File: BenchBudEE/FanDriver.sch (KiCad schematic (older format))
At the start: 0 parts

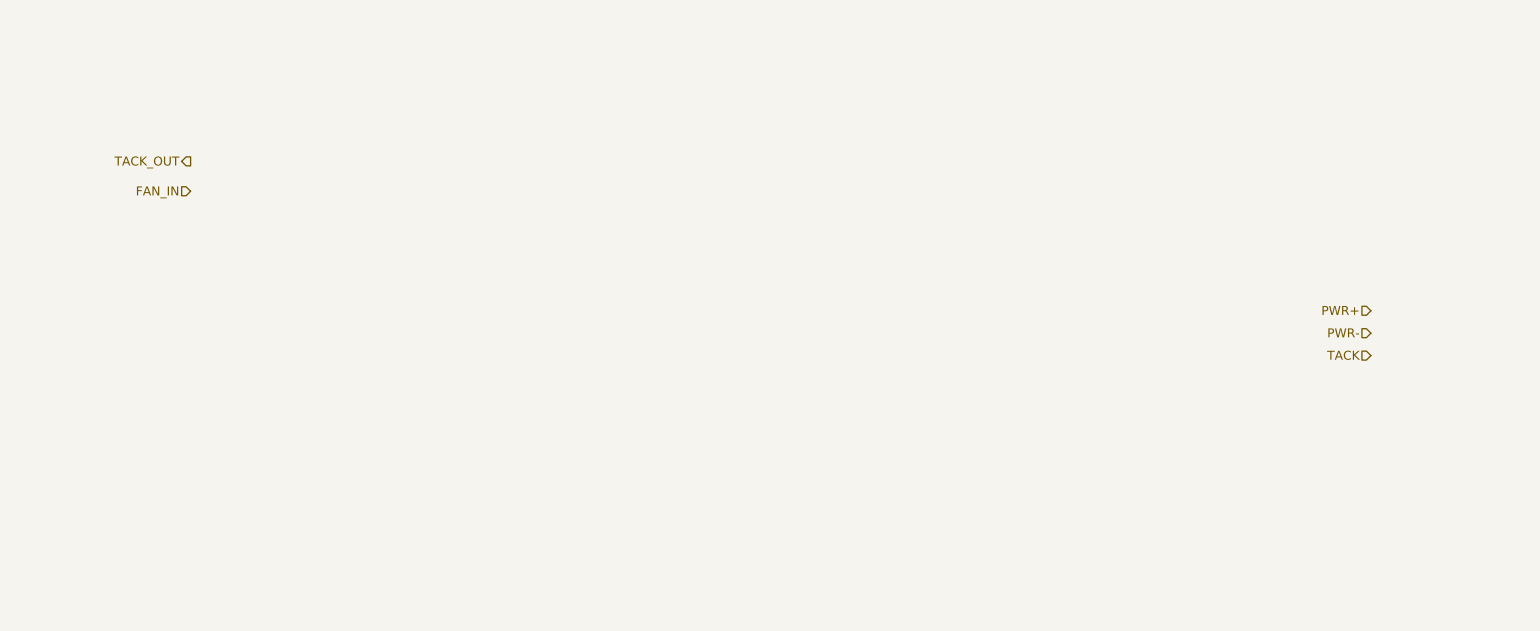
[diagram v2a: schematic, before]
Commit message: Created Fan Module block diagram + added new I/O + minor spelling corrections
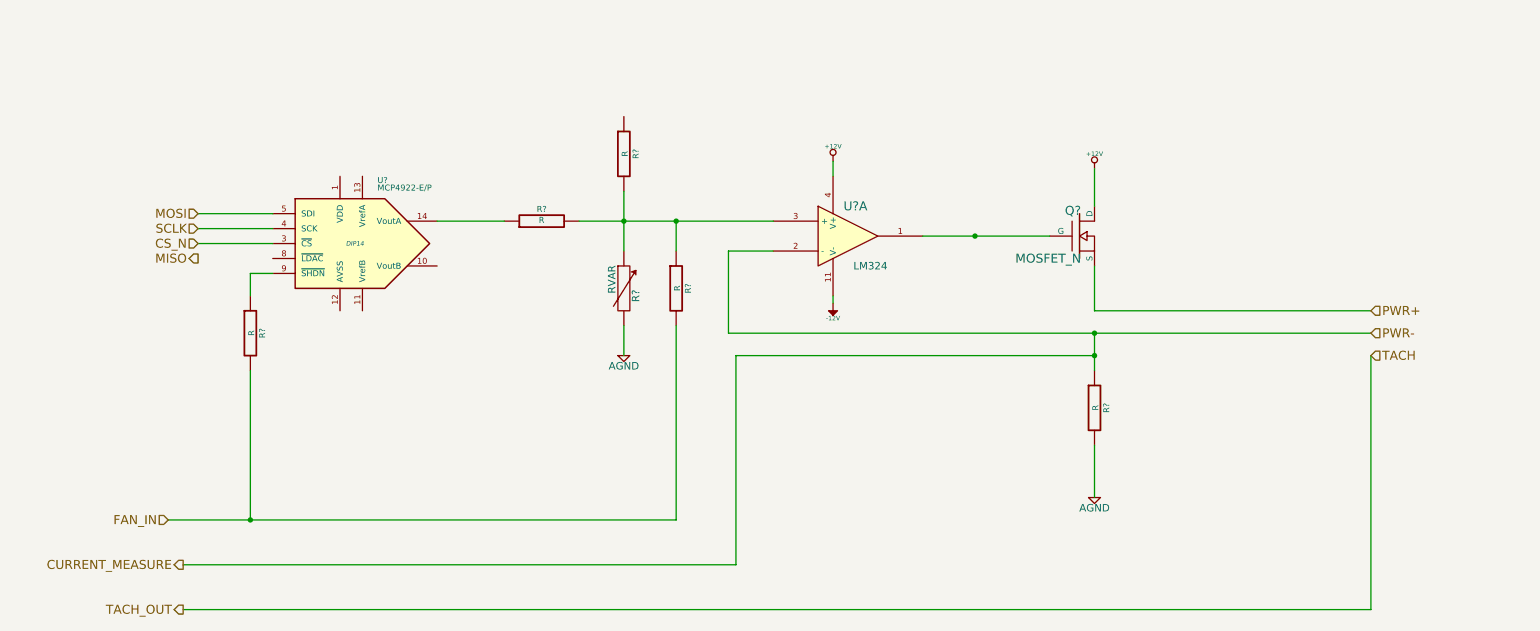
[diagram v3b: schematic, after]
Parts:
- added Q?: MOSFET_N, ~, symbol MOSFET_N
- added R? (x5): R, ~, symbol R
- added R?: RVAR, ~, symbol RVAR
- added U?: LM324, symbol LM324
- added U?: MCP4922-E/P, DIP14, symbol MCP4922-E/P
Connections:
- net FAN_IN: now also R?.2, R?.2
- net PWR+: now also Q?.S
- new net: Q?.G, U?.1
- new net: R?.1, R?.1, R?.2, R?.2, U?.3 (+)
- new net: R?.1, U?.14 (VoutA)
- new net: R?.1, U?.9 (~SHDN~)
- new net +12V: Q?.D, U?.4 (V+)
- new net -12V: U?.11 (V-)
- new net AGND: R?.2, R?.2
- new net CS_N: U?.3 (~CS~)
- new net CURRENT_MEASURE: R?.1, U?.2 (-)
- new net MOSI: U?.5 (SDI)
- new net SCLK: U?.4 (SCK)

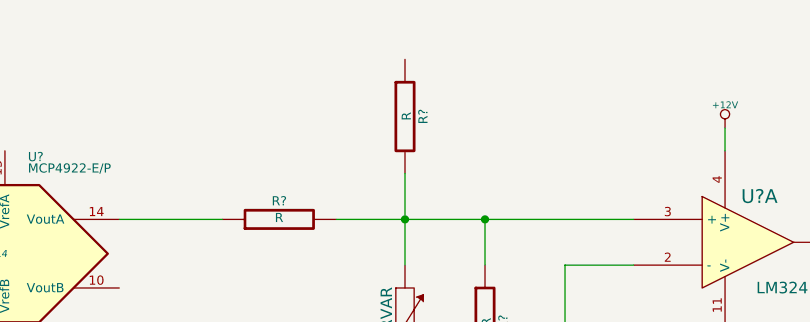
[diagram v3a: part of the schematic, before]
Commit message: Created Relay block diagram
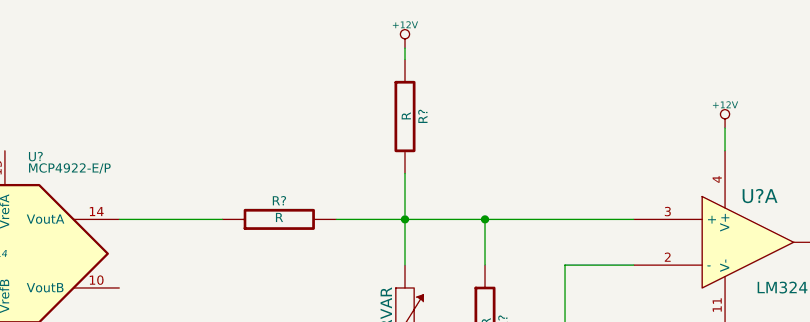
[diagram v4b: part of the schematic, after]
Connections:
- net +12V: now also R?.1
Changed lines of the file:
@@
 LIBS:contrib
 LIBS:valves
+LIBS:CE Library
 LIBS:BenchBudEE-cache
 EELAYER 27 0
@@
 $Descr A4 11693 8268
 encoding utf-8
-Sheet 3 8
+Sheet 7 8
 Title ""
 Date "5 feb 2014"
@@
 Wire Wire Line
 	7800 1600 7800 1850
+$Comp
+L +12V #PWR?
+U 1 1 52F2ACAE
+P 4650 1200
+F 0 "#PWR?" H 4650 1150 20  0001 C CNN
+F 1 "+12V" H 4650 1300 30  0000 C CNN
+F 2 "" H 4650 1200 60  0000 C CNN
+F 3 "" H 4650 1200 60  0000 C CNN
+	1    4650 1200
+	1    0    0    -1
+$EndComp
+Wire Wire Line
+	4650 1250 4650 1200
 $EndSCHEMATC

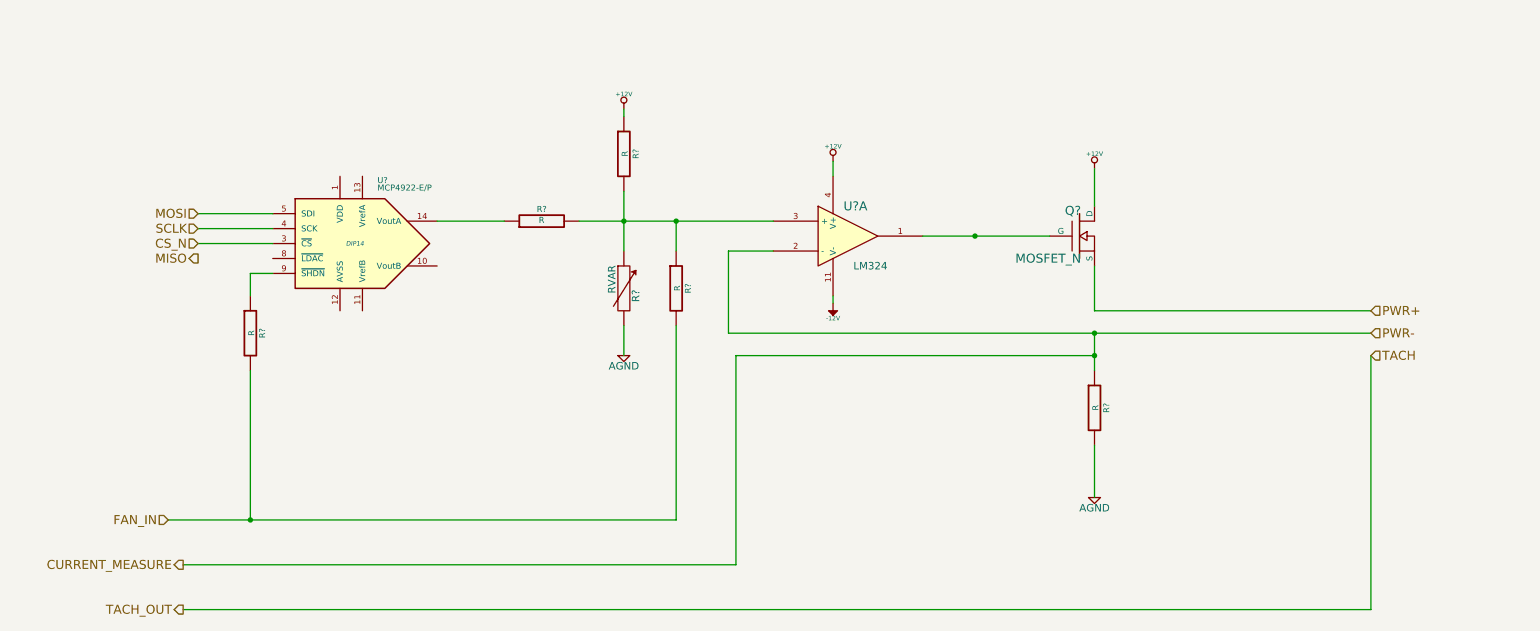
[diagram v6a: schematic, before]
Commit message: Schematic modules connected together and to arduino pins
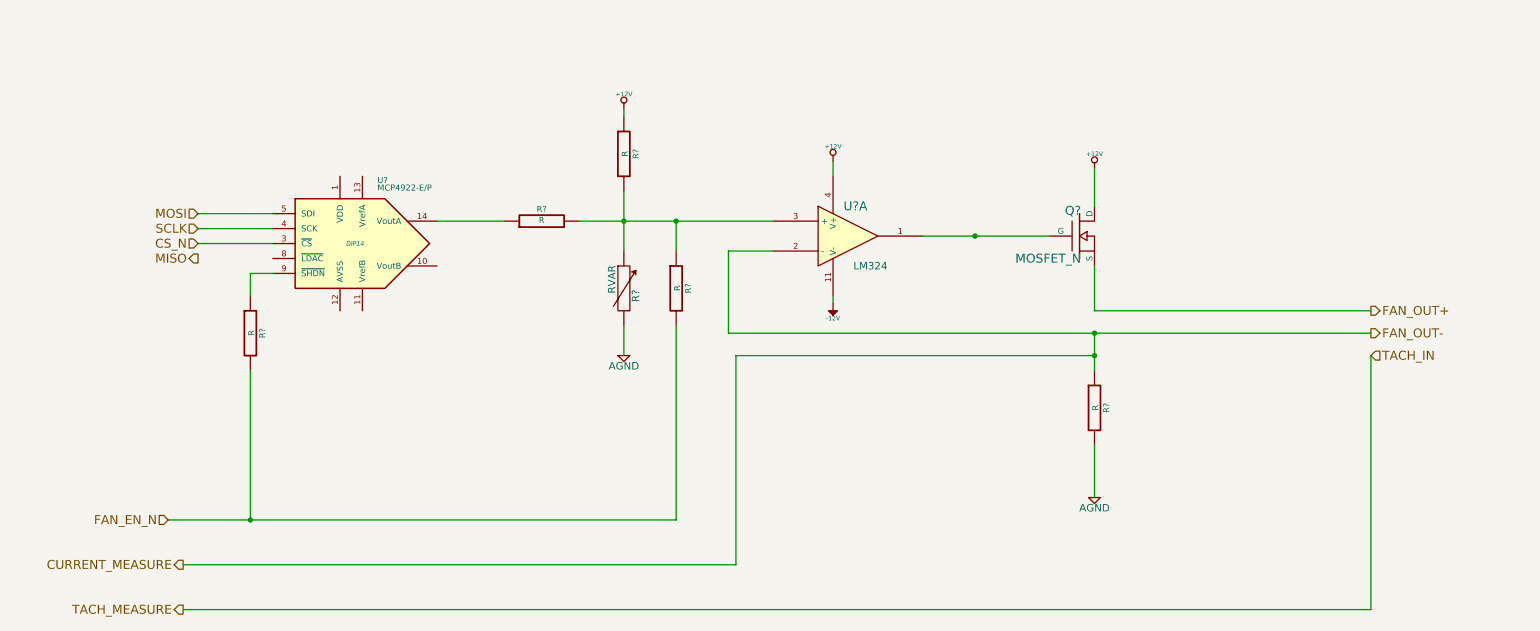
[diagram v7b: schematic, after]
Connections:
- net FAN_IN renamed FAN_EN_N
- net PWR+ renamed FAN_OUT+
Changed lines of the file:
@@
 LIBS:valves
 LIBS:CE Library
+LIBS:atx_24pin_power
 LIBS:BenchBudEE-cache
 EELAYER 27 0
@@
 $Descr A4 11693 8268
 encoding utf-8
-Sheet 7 9
+Sheet 6 9
 Title ""
-Date "6 feb 2014"
+Date "8 feb 2014"
 Rev ""
 Comp ""
@@
 Comment4 ""
 $EndDescr
-Text HLabel 9650 2550 2    60   Input ~ 0
-PWR+
-Text HLabel 9650 2700 2    60   Input ~ 0
-PWR-
+Text HLabel 9650 2550 2    60   Output ~ 0
+FAN_OUT+
+Text HLabel 9650 2700 2    60   Output ~ 0
+FAN_OUT-
 Text HLabel 9650 2850 2    60   Input ~ 0
-TACH
+TACH_IN
 Text HLabel 1700 4550 0    60   Output ~ 0
-TACH_OUT
+TACH_MEASURE
 Text HLabel 1600 3950 0    60   Input ~ 0
-FAN_IN
+FAN_EN_N
 $Comp
 L LM324 U?

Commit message: Parts added to relay module. Schematic tidied up.
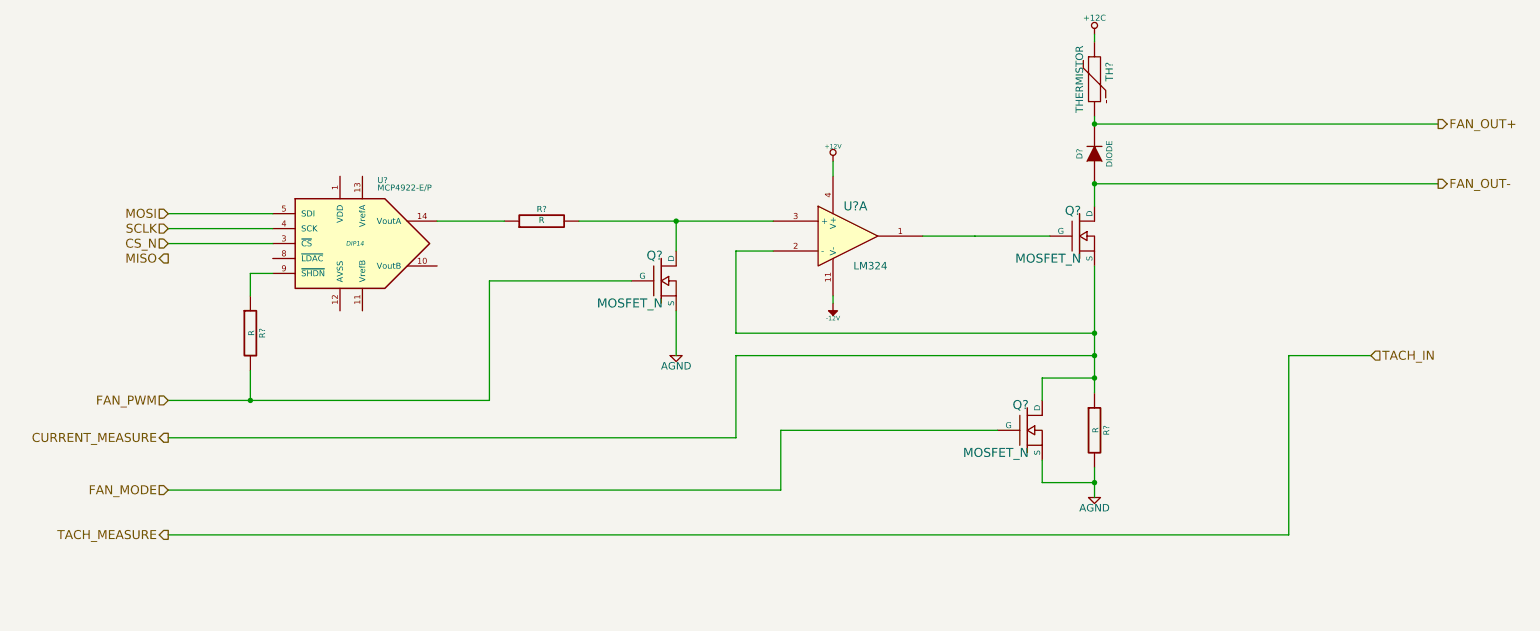
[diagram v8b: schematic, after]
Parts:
- removed R? (x2): R, ~, symbol R
- removed R?: RVAR, ~, symbol RVAR
- added D?: DIODE, ~, symbol DIODE
- added Q? (x2): MOSFET_N, ~, symbol MOSFET_N
- added TH?: THERMISTOR, ~, symbol THERMISTOR
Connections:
- net +12V: no longer Q?.D
- net AGND: now also Q?.S, Q?.S
- net CURRENT_MEASURE: now also Q?.S, Q?.D
- net FAN_OUT+: now also D?.2 (K), TH?.2; no longer Q?.S
- net at R?.2, U?.3 (+): now also Q?.D
- net FAN_EN_N renamed FAN_PWM
- net FAN_PWM: now also Q?.G
- new net +12C: TH?.1
- new net FAN_MODE: Q?.G
- new net FAN_OUT-: D?.1 (A), Q?.D
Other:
- moved on the sheet: R?
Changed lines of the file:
@@
 Sheet 6 9
 Title ""
-Date "8 feb 2014"
+Date "19 feb 2014"
 Rev ""
 Comp ""
@@
 Comment4 ""
 $EndDescr
-Text HLabel 9650 2550 2    60   Output ~ 0
+Text HLabel 10100 1300 2    60   Output ~ 0
 FAN_OUT+
-Text HLabel 9650 2700 2    60   Output ~ 0
+Text HLabel 10100 1700 2    60   Output ~ 0
 FAN_OUT-
 Text HLabel 9650 2850 2    60   Input ~ 0
 TACH_IN
-Text HLabel 1700 4550 0    60   Output ~ 0
+Text HLabel 1600 4050 0    60   Output ~ 0
 TACH_MEASURE
-Text HLabel 1600 3950 0    60   Input ~ 0
-FAN_EN_N
+Text HLabel 1600 3150 0    60   Input ~ 0
+FAN_PWM
 $Comp
 L LM324 U?
@@
 	1    0    0    -1
 $EndComp
-Wire Wire Line
-	5650 2150 5350 2150
-Wire Wire Line
-	5350 2150 5350 2700
-Wire Wire Line
-	6650 2050 7500 2050
-Connection ~ 7000 2050
-Wire Wire Line
-	7800 2250 7800 2550
-Wire Wire Line
-	7800 2550 9650 2550
 $Comp
 L R R?
 U 1 1 52F28A75
-P 7800 3200
-F 0 "R?" V 7880 3200 40  0000 C CNN
-F 1 "R" V 7807 3201 40  0000 C CNN
-F 2 "~" V 7730 3200 30  0000 C CNN
-F 3 "~" H 7800 3200 30  0000 C CNN
-	1    7800 3200
+P 7800 3350
+F 0 "R?" V 7880 3350 40  0000 C CNN
+F 1 "R" V 7807 3351 40  0000 C CNN
+F 2 "~" V 7730 3350 30  0000 C CNN
+F 3 "~" H 7800 3350 30  0000 C CNN
+	1    7800 3350
 	1    0    0    -1
 $EndComp
@@
 	1    0    0    -1
 $EndComp
-Wire Wire Line
-	5350 2700 9650 2700
-Wire Wire Line
-	7800 2950 7800 2700
-Connection ~ 7800 2700
-Wire Wire Line
-	7800 3450 7800 3800
 $Comp
 L -12V #PWR?
@@
 	1    0    0    1
 $EndComp
-Wire Wire Line
-	6050 2450 6050 2500
-Wire Wire Line
-	6050 1650 6050 1550
-Wire Wire Line
-	4350 1950 5650 1950
-$Comp
-L R R?
-U 1 1 52F28ADF
-P 4650 1500
-F 0 "R?" V 4730 1500 40  0000 C CNN
-F 1 "R" V 4657 1501 40  0000 C CNN
-F 2 "~" V 4580 1500 30  0000 C CNN
-F 3 "~" H 4650 1500 30  0000 C CNN
-	1    4650 1500
-	1    0    0    -1
-$EndComp
-Wire Wire Line
-	4650 1750 4650 2150
 $Comp
 L AGND #PWR?
 U 1 1 52F28AF3
-P 4650 2850
-F 0 "#PWR?" H 4650 2850 40  0001 C CNN
-F 1 "AGND" H 4650 2780 50  0000 C CNN
-F 2 "" H 4650 2850 60  0000 C CNN
-F 3 "" H 4650 2850 60  0000 C CNN
-	1    4650 2850
-	1    0    0    -1
-$EndComp
-$Comp
-L RVAR R?
-U 1 1 52F28AFB
-P 4650 2400
-F 0 "R?" V 4730 2350 50  0000 C CNN
-F 1 "RVAR" V 4570 2460 50  0000 C CNN
-F 2 "~" H 4650 2400 60  0000 C CNN
-F 3 "~" H 4650 2400 60  0000 C CNN
-	1    4650 2400
-	1    0    0    -1
-$EndComp
-Connection ~ 4650 1950
-Wire Wire Line
-	4650 2850 4650 2650
+P 5000 2850
+F 0 "#PWR?" H 5000 2850 40  0001 C CNN
+F 1 "AGND" H 5000 2780 50  0000 C CNN
+F 2 "" H 5000 2850 60  0000 C CNN
+F 3 "" H 5000 2850 60  0000 C CNN
+	1    5000 2850
+	1    0    0    -1
+$EndComp
 $Comp
 L MCP4922-E/P U?
@@
 	1    0    0    -1
 $EndComp
-Wire Wire Line
-	9650 4550 9650 2850
-Wire Wire Line
-	1700 4550 9650 4550
-Text HLabel 1700 4250 0    60   Output ~ 0
+Text HLabel 1600 3400 0    60   Output ~ 0
 CURRENT_MEASURE
-Wire Wire Line
-	7800 2850 5400 2850
-Wire Wire Line
-	5400 2850 5400 4250
-Wire Wire Line
-	5400 4250 1700 4250
-Connection ~ 7800 2850
-$Comp
-L R R?
-U 1 1 52F28B8D
-P 5000 2400
-F 0 "R?" V 5080 2400 40  0000 C CNN
-F 1 "R" V 5007 2401 40  0000 C CNN
-F 2 "~" V 4930 2400 30  0000 C CNN
-F 3 "~" H 5000 2400 30  0000 C CNN
-	1    5000 2400
-	1    0    0    -1
-$EndComp
-Wire Wire Line
-	5000 2150 5000 1950
-Connection ~ 5000 1950
-Wire Wire Line
-	5000 2650 5000 3950
-Wire Wire Line
-	5000 3950 1600 3950
 $Comp
 L R R?
@@
 	0    -1   -1   0
 $EndComp
-Wire Wire Line
-	3850 1950 3400 1950
-Text HLabel 1800 1900 0    60   Input ~ 0
+Text HLabel 1600 1900 0    60   Input ~ 0
 MOSI
-Text HLabel 1800 2200 0    60   Output ~ 0
+Text HLabel 1600 2200 0    60   Output ~ 0
 MISO
-Text HLabel 1800 2000 0    60   Input ~ 0
+Text HLabel 1600 2000 0    60   Input ~ 0
 SCLK
-Text HLabel 1800 2100 0    60   Input ~ 0
+Text HLabel 1600 2100 0    60   Input ~ 0
 CS_N
-Wire Wire Line
-	1800 1900 2300 1900
-Wire Wire Line
-	2300 2000 1800 2000
-Wire Wire Line
-	1800 2100 2300 2100
 $Comp
 L R R?
@@
 	1    0    0    -1
 $EndComp
+$Comp
+L MOSFET_N Q?
+U 1 1 52F7E547
+P 7350 3350
+F 0 "Q?" H 7360 3520 60  0000 R CNN
+F 1 "MOSFET_N" H 7360 3200 60  0000 R CNN
+F 2 "~" H 7350 3350 60  0000 C CNN
+F 3 "~" H 7350 3350 60  0000 C CNN
+	1    7350 3350
+	1    0    0    -1
+$EndComp
+$Comp
+L THERMISTOR TH?
+U 1 1 52F7E559
+P 7800 1000
+F 0 "TH?" V 7900 1050 50  0000 C CNN
+F 1 "THERMISTOR" V 7700 1000 50  0000 C CNN
+F 2 "~" H 7800 1000 60  0000 C CNN
+F 3 "~" H 7800 1000 60  0000 C CNN
+	1    7800 1000
+	1    0    0    -1
+$EndComp
+$Comp
+L DIODE D?
+U 1 1 52F7E659
+P 7800 1500
+F 0 "D?" H 7800 1600 40  0000 C CNN
+F 1 "DIODE" H 7800 1400 40  0000 C CNN
+F 2 "~" H 7800 1500 60  0000 C CNN
+F 3 "~" H 7800 1500 60  0000 C CNN
+	1    7800 1500
+	0    -1   -1   0
+$EndComp
+Wire Wire Line
+	5650 2150 5400 2150
+Wire Wire Line
+	5400 2150 5400 2700
+Wire Wire Line
+	6650 2050 7000 2050
+Wire Wire Line
+	7000 2050 7500 2050
+Wire Wire Line
+	7800 2250 7800 2700
+Wire Wire Line
+	7800 2700 7800 2850
+Wire Wire Line
+	7800 2850 7800 3000
+Wire Wire Line
+	7800 3000 7800 3100
+Connection ~ 7800 2700
+Wire Wire Line
+	7800 3600 7800 3700
+Wire Wire Line
+	7800 3700 7800 3800
+Wire Wire Line
+	6050 2450 6050 2500
+Wire Wire Line
+	6050 1650 6050 1550
+Wire Wire Line
+	4350 1950 5000 1950
+Wire Wire Line
+	5000 1950 5650 1950
+Wire Wire Line
+	7800 2850 5400 2850
+Wire Wire Line
+	5400 2850 5400 3400
+Wire Wire Line
+	5400 3400 1600 3400
+Connection ~ 7800 2850
+Wire Wire Line
+	3850 1950 3400 1950
+Wire Wire Line
+	1600 1900 2300 1900
+Wire Wire Line
+	2300 2000 1600 2000
+Wire Wire Line
+	1600 2100 2300 2100
 Wire Wire Line
 	2300 2300 2150 2300
@@
 	2150 2300 2150 2450
 Wire Wire Line
-	2150 2950 2150 3950
-Connection ~ 2150 3950
-$Comp
-L +12V #PWR?
-U 1 1 52F28CA6
-P 7800 1600
-F 0 "#PWR?" H 7800 1550 20  0001 C CNN
-F 1 "+12V" H 7800 1700 30  0000 C CNN
-F 2 "" H 7800 1600 60  0000 C CNN
-F 3 "" H 7800 1600 60  0000 C CNN
-	1    7800 1600
-	1    0    0    -1
-$EndComp
-Wire Wire Line
-	7800 1600 7800 1850
-$Comp
-L +12V #PWR?
-U 1 1 52F2ACAE
-P 4650 1200
-F 0 "#PWR?" H 4650 1150 20  0001 C CNN
-F 1 "+12V" H 4650 1300 30  0000 C CNN
-F 2 "" H 4650 1200 60  0000 C CNN
-F 3 "" H 4650 1200 60  0000 C CNN
-	1    4650 1200
-	1    0    0    -1
-$EndComp
-Wire Wire Line
-	4650 1250 4650 1200
+	2150 2950 2150 3150
+Connection ~ 2150 3150
+Wire Wire Line
+	10100 1700 7800 1700
+Wire Wire Line
+	7800 1700 7800 1700
+Wire Wire Line
+	7800 1700 7800 1850
+Wire Wire Line
+	7800 1250 7800 1300
+Wire Wire Line
+	7800 1300 7800 1300
+Wire Wire Line
+	7800 1300 10100 1300
+Wire Wire Line
+	7800 1300 7800 1300
+Connection ~ 7800 1300
+Wire Wire Line
+	7800 1700 7800 1700
+Connection ~ 7800 1700
+Wire Wire Line
+	7450 3150 7450 3000
+Wire Wire Line
+	7450 3000 7800 3000
+Connection ~ 7800 3000
+Wire Wire Line
+	7450 3550 7450 3700
+Wire Wire Line
+	7450 3700 7800 3700
+Connection ~ 7800 3700
+Wire Wire Line
+	5400 2700 7800 2700
+Wire Wire Line
+	1600 4050 9100 4050
+Wire Wire Line
+	9100 4050 9100 2850
+Wire Wire Line
+	9100 2850 9650 2850
+$Comp
+L MOSFET_N Q?
+U 1 1 52F7E89F
+P 4900 2350
+F 0 "Q?" H 4910 2520 60  0000 R CNN
+F 1 "MOSFET_N" H 4910 2200 60  0000 R CNN
+F 2 "~" H 4900 2350 60  0000 C CNN
+F 3 "~" H 4900 2350 60  0000 C CNN
+	1    4900 2350
+	1    0    0    -1
+$EndComp
+Wire Wire Line
+	1600 3150 2150 3150
+Wire Wire Line
+	2150 3150 3750 3150
+Wire Wire Line
+	3750 2350 4700 2350
+Wire Wire Line
+	5000 2550 5000 2850
+Wire Wire Line
+	3750 3150 3750 2350
+Wire Wire Line
+	5000 2150 5000 1950
+Connection ~ 5000 1950
+Wire Wire Line
+	7150 3350 5700 3350
+Wire Wire Line
+	5700 3350 5700 3750
+Wire Wire Line
+	5700 3750 1600 3750
+Text HLabel 1600 3750 0    60   Input ~ 0
+FAN_MODE
+$Comp
+L +12C #PWR?
+U 1 1 52F7ED72
+P 7800 700
+F 0 "#PWR?" H 7800 670 30  0001 C CNN
+F 1 "+12C" H 7800 810 40  0000 C CNN
+F 2 "" H 7800 700 60  0000 C CNN
+F 3 "" H 7800 700 60  0000 C CNN
+	1    7800 700
+	1    0    0    -1
+$EndComp
+Wire Wire Line
+	7800 700  7800 750
 $EndSCHEMATC
